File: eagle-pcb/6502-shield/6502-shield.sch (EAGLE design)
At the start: 45 parts, among them SW1 MCSLPT4644B1TR-TACT-SW, SW2 PCM12SMTR-SPDT-RIGHT-ANG, SW3 MCSLPT4644B1TR-TACT-SW, U1 AT28C256TSOP-28, U2 W65C02S, U3 AS6C62256, U4 W65C22, U5 MACHXO-FPGA100TQFP

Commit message: fully routed, getting close
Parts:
- removed D10, D8, D9: ACDC02-41SGWA-DUAL-7SEG, 6502-shield:ACDC02-41SGWA-DUAL-7SEG
- removed R10, R11, R12, R13, R14, R15, R16, R17: 330, rcl:R-US_R0402
- removed U5: MACHXO-FPGA100TQFP, 6502-shield:MACHXO-FPGA100TQFP
- added C1, C2, C5, C6, C7: 0.1uF, rcl:C-USC0402
- added FPGA: MACHXO-FPGA100TQFP, 6502-shield:MACHXO-FPGA100TQFP
- D1, D2, D3, D4, D5, D6, D7: value (none) -> RED
- renumbered SJ1 to J1, SW1 to PB_RESET, SW2 to SW_RUNHALT, SW3 to PB_STEP, U$1 to EXT_XO, U1 to EEPROM, U2 to CPU, U3 to RAM, U4 to PIO
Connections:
- removed net DIGIT1_EN: D8.1EN, U5_BANK1_TOP.PT3D
- removed net DIGIT2_EN: D8.2EN, U5_BANK1_TOP.PT3C
- removed net DIGIT3_EN: D9.1EN, U5_BANK1_TOP.PT3B
- removed net DIGIT4_EN: D9.2EN, U5_BANK1_TOP.PT3A
- removed net DIGIT5_EN: D10.1EN, U5_BANK1_TOP.PT2F
- removed net DIGIT6_EN: D10.2EN, U5_BANK1_TOP.PT2E
- removed net DIGIT_A: R10.2, U5_BANK1_TOP.PT5B
- removed net DIGIT_B: R11.2, U5_BANK1_TOP.PT5A
- removed net DIGIT_C: R12.2, U5_BANK1_TOP.PT4F
- removed net DIGIT_D: R13.2, U5_BANK1_TOP.PT4E
- removed net DIGIT_DP: R17.2, U5_BANK1_TOP.PT4A
- removed net DIGIT_E: R14.2, U5_BANK1_TOP.PT4D
- removed net DIGIT_F: R15.2, U5_BANK1_TOP.PT4C
- removed net DIGIT_G: R16.2, U5_BANK1_TOP.PT4B
- removed net N$23: D10.1A, D10.2A, D8.1A, D8.2A, D9.1A, D9.2A, R10.1
- removed net N$24: D10.1B, D10.2B, D8.1B, D8.2B, D9.1B, D9.2B, R11.1
- removed net N$25: D10.1C, D10.2C, D8.1C, D8.2C, D9.1C, D9.2C, R12.1
- removed net N$26: D10.1D, D10.2D, D8.1D, D8.2D, D9.1D, D9.2D, R13.1
- removed net N$27: D10.1E, D10.2E, D8.1E, D8.2E, D9.1E, D9.2E, R14.1
- removed net N$28: D10.1F, D10.2F, D8.1F, D8.2F, D9.1F, D9.2F, R15.1
- removed net N$29: D10.1G, D10.2G, D8.1G, D8.2G, D9.1G, D9.2G, R16.1
- removed net N$30: D10.1DP, D10.2DP, D8.1DP, D8.2DP, D9.1DP, D9.2DP, R17.1
- removed net ROM_PGM: PCB1.45, U5_BANK0_BOTTOM.PB2D
- new net EEPROM_PGM: FPGA_BANK0_BOTTOM.PB2D, PCB1.23
- net A0: now also FPGA_BANK1_RIGHT.PR8A, PCB1.44; no longer PCB1.22, U5_BANK1_RIGHT.PR8A
- net A1: now also FPGA_BANK1_RIGHT.PR7D, PCB1.45; no longer PCB1.24, U5_BANK1_RIGHT.PR7D
- net A10: now also FPGA_BANK1_RIGHT.PR5A, PCB1.34; no longer PCB1.42, U5_BANK1_RIGHT.PR5A
- net A11: now also FPGA_BANK1_RIGHT.PR4B, PCB1.35; no longer PCB1.44, U5_BANK1_RIGHT.PR4B
- net A12: now also FPGA_BANK1_RIGHT.PR4A, PCB1.32; no longer PCB1.46, U5_BANK1_RIGHT.PR4A
- net A13: now also FPGA_BANK1_RIGHT.PR3D, PCB1.33; no longer PCB1.48, U5_BANK1_RIGHT.PR3D
- net A14: now also FPGA_BANK1_RIGHT.PR3C, PCB1.30; no longer PCB1.50, U5_BANK1_RIGHT.PR3C
- net A15: now also FPGA_BANK1_RIGHT.PR3B, PCB1.31; no longer PCB1.52, U5_BANK1_RIGHT.PR3B
- net A2: now also FPGA_BANK1_RIGHT.PR7C, PCB1.42; no longer PCB1.26, U5_BANK1_RIGHT.PR7C
- net A3: now also FPGA_BANK1_RIGHT.PR7B, PCB1.43; no longer PCB1.28, U5_BANK1_RIGHT.PR7B
- net A4: now also FPGA_BANK1_RIGHT.PR7A, PCB1.40; no longer PCB1.30, U5_BANK1_RIGHT.PR7A
- net A5: now also FPGA_BANK1_RIGHT.PR6B, PCB1.41; no longer PCB1.32, U5_BANK1_RIGHT.PR6B
- net A6: now also FPGA_BANK1_RIGHT.PR6A, PCB1.38; no longer PCB1.34, U5_BANK1_RIGHT.PR6A
- net A7: now also FPGA_BANK1_RIGHT.PR5D, PCB1.39; no longer PCB1.36, U5_BANK1_RIGHT.PR5D
- net A8: now also FPGA_BANK1_RIGHT.PR5C, PCB1.36; no longer PCB1.38, U5_BANK1_RIGHT.PR5C
- net A9: now also FPGA_BANK1_RIGHT.PR5B, PCB1.37; no longer PCB1.40, U5_BANK1_RIGHT.PR5B
- net BE: now also FPGA_BANK0_BOTTOM.PB3C; no longer U5_BANK0_BOTTOM.PB3C
- net CLK: now also FPGA_BANK0_BOTTOM.PB3B, PCB1.27; no longer PCB1.43, U5_BANK0_BOTTOM.PB3B
- net CLK_SEL: now also FPGA_BANK0_LEFT.PL7B; no longer U5_BANK0_LEFT.PL7B
- net D0: now also FPGA_BANK0_BOTTOM.PB4C, PCB1.52; no longer PCB1.23, U5_BANK0_BOTTOM.PB4C
- net D1: now also FPGA_BANK0_BOTTOM.PB4D, PCB1.53; no longer PCB1.25, U5_BANK0_BOTTOM.PB4D
- net D2: now also FPGA_BANK0_BOTTOM.PB5A, PCB1.50; no longer PCB1.27, U5_BANK0_BOTTOM.PB5A
- net D3: now also FPGA_BANK0_BOTTOM.PB5C, PCB1.51; no longer PCB1.29, U5_BANK0_BOTTOM.PB5C
- net D4: now also FPGA_BANK0_BOTTOM.PB5D, PCB1.48; no longer PCB1.31, U5_BANK0_BOTTOM.PB5D
- net D5: now also FPGA_BANK1_RIGHT.PR9B, PCB1.49; no longer PCB1.33, U5_BANK1_RIGHT.PR9B
- net D6: now also FPGA_BANK1_RIGHT.PR9A, PCB1.46; no longer PCB1.35, U5_BANK1_RIGHT.PR9A
- net D7: now also FPGA_BANK1_RIGHT.PR8B, PCB1.47; no longer PCB1.37, U5_BANK1_RIGHT.PR8B
- net DMA: now also FPGA_BANK0_BOTTOM.PB2C, PCB1.22; no longer PCB1.47, U5_BANK0_BOTTOM.PB2C
- net GND: now also C1.2, C2.2, C5.2, C6.2, C7.2, FPGA_CORE.GND; no longer U5_CORE.GND
- net IO_EN: now also FPGA_BANK0_BOTTOM.PB3A; no longer U5_BANK0_BOTTOM.PB3A
- net IRQN: now also FPGA_BANK0_BOTTOM.PB4B; no longer U5_BANK0_BOTTOM.PB4B
- net N$1: now also FPGA_CORE.SLEEPN; no longer U5_CORE.SLEEPN
- net N$10: now also FPGA_BANK0_LEFT.PL2B; no longer U5_BANK0_LEFT.PL2B
- net N$11: now also FPGA_BANK0_LEFT.PL3A; no longer U5_BANK0_LEFT.PL3A
- net N$16: now also FPGA_BANK1_TOP.PT2A; no longer U5_BANK1_TOP.PT2A
- net N$17: now also FPGA_BANK1_TOP.PT2B; no longer U5_BANK1_TOP.PT2B
- net N$18: now also FPGA_BANK1_TOP.PT2C; no longer U5_BANK1_TOP.PT2C
- net N$19: now also FPGA_BANK1_TOP.PT2D; no longer U5_BANK1_TOP.PT2D
- net N$2: now also FPGA_BANK0_LEFT.PL3C; no longer U5_BANK0_LEFT.PL3C
- net N$3: now also FPGA_CORE.GSRN_PL5D; no longer U5_CORE.GSRN_PL5D
- net N$34: now also FPGA_BANK0_LEFT.PL7A; no longer U5_BANK0_LEFT.PL7A
- net N$4: now also FPGA_JTAG.TDO; no longer U5_JTAG.TDO
- net N$5: now also FPGA_JTAG.TMS; no longer U5_JTAG.TMS
- net N$6: now also FPGA_JTAG.TDI; no longer U5_JTAG.TDI
- net N$7: now also FPGA_JTAG.TCK; no longer U5_JTAG.TCK
- net N$8: now also FPGA_BANK0_LEFT.PL3B; no longer U5_BANK0_LEFT.PL3B
- net N$9: now also FPGA_BANK0_LEFT.PL2A; no longer U5_BANK0_LEFT.PL2A
- net OE: now also FPGA_BANK1_RIGHT.PR2B, PCB1.25; no longer PCB1.39, U5_BANK1_RIGHT.PR2B
- net RAM_EN: now also FPGA_BANK1_RIGHT.PR2A; no longer U5_BANK1_RIGHT.PR2A
- net RESETN: now also FPGA_BANK0_BOTTOM.PB3D; no longer U5_BANK0_BOTTOM.PB3D
- net ROM_EN: now also FPGA_BANK1_TOP.PT5C; no longer U5_BANK1_TOP.PT5C
- net RW: now also FPGA_BANK0_BOTTOM.PB4A; no longer U5_BANK0_BOTTOM.PB4A
- net VCC: now also C1.1, C2.1, C5.1, C6.1, C7.1, FPGA_CORE.VCC, FPGA_CORE.VCC_AUX, FPGA_CORE.VCC_IO_0, FPGA_CORE.VCC_IO_1; no longer U5_CORE.VCC, U5_CORE.VCC_AUX, U5_CORE.VCC_IO_0, U5_CORE.VCC_IO_1
- net WE: now also FPGA_BANK1_RIGHT.PR3A, PCB1.29; no longer PCB1.41, U5_BANK1_RIGHT.PR3A
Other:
- moved on the sheet: C3, C4, D3, D4, D6, D7, JP1, R6, R7, R8, R9

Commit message: This should be ready to send out.
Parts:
- EEPROM: value AT28C256TSOP-28 -> AT28BV256TSOP-28; device 6502-shield:AT28C256TSOP-28 -> 6502-shield:AT28BV256TSOP-28
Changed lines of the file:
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@@
 </classes>
 <parts>
-<part name="PCB1" library="E14_Arduino_revC" library_urn="urn:adsk.eagle:library:18477430" deviceset="ARDUINO_MEGA2560" device="" package3d_urn="urn:adsk.eagle:package:18477461/4"/>
+<part name="PCB1" library="E14_Arduino_revC" library_urn="urn:adsk.eagle:library:18477430" deviceset="ARDUINO_MEGA2560" device="" package3d_urn="urn:adsk.eagle:package:18477461/5"/>
 <part name="PB_RESET" library="6502-shield" library_urn="urn:adsk.eagle:library:18477216" deviceset="MCSLPT4644B1TR-TACT-SW" device="" package3d_urn="urn:adsk.eagle:package:18592201/6"/>
 <part name="SW_RUNHALT" library="6502-shield" library_urn="urn:adsk.eagle:library:18477216" deviceset="PCM12SMTR-SPDT-RIGHT-ANG" device="" package3d_urn="urn:adsk.eagle:package:18622137/7"/>
@@
 <part name="P+17" library="supply1" library_urn="urn:adsk.eagle:library:371" deviceset="VCC" device=""/>
 <part name="GND19" library="supply1" library_urn="urn:adsk.eagle:library:371" deviceset="GND" device=""/>
-<part name="EEPROM" library="6502-shield" library_urn="urn:adsk.eagle:library:18477216" deviceset="AT28C256" device="TSOP-28" package3d_urn="urn:adsk.eagle:package:18436546/2"/>
+<part name="EEPROM" library="6502-shield" library_urn="urn:adsk.eagle:library:18477216" deviceset="AT28BV256" device="TSOP-28" package3d_urn="urn:adsk.eagle:package:18436546/2"/>
 <part name="FRAME2" library="frames" library_urn="urn:adsk.eagle:library:229" deviceset="FRAME_A_L" device="" value="6502-shield"/>
 <part name="P+19" library="supply1" library_urn="urn:adsk.eagle:library:371" deviceset="VCC" device=""/>

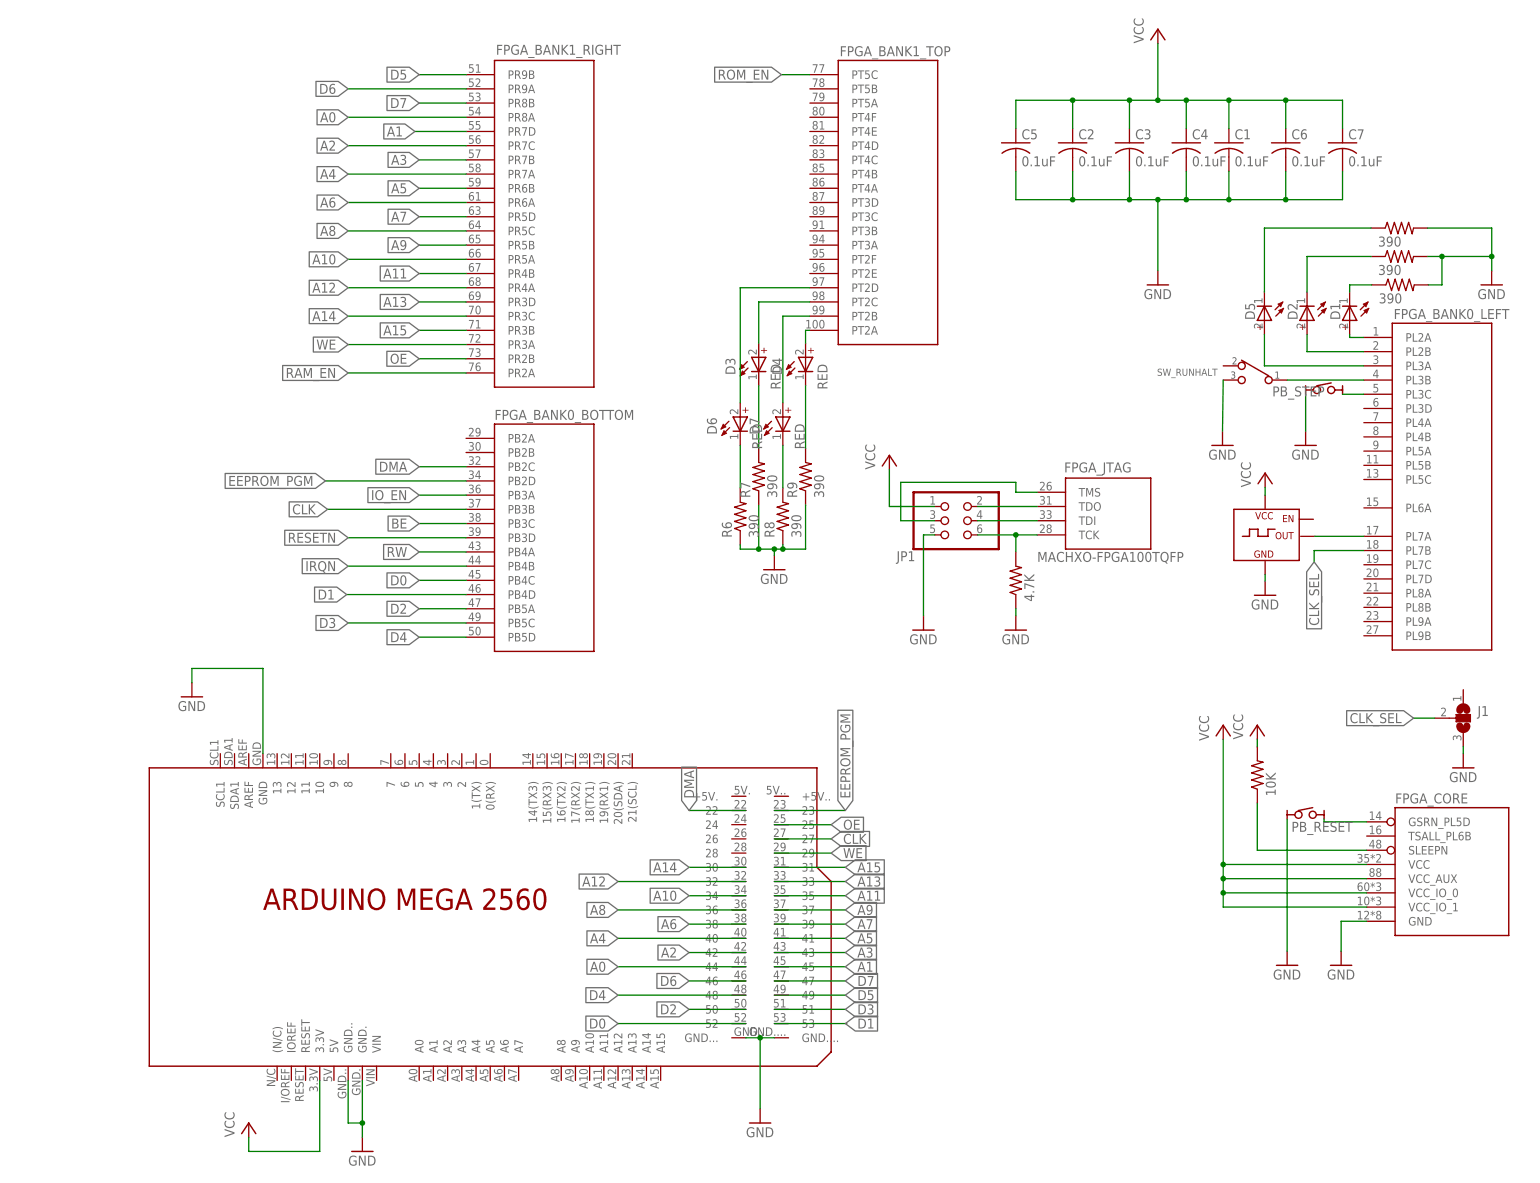
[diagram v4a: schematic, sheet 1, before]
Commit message: Fixed problems with FPGA pinout in component library, updated schematic and cleaned it up a bunch.  Fixed external clock not coming into FPGA on dedicated clock net pin. More schematic work on the list still.
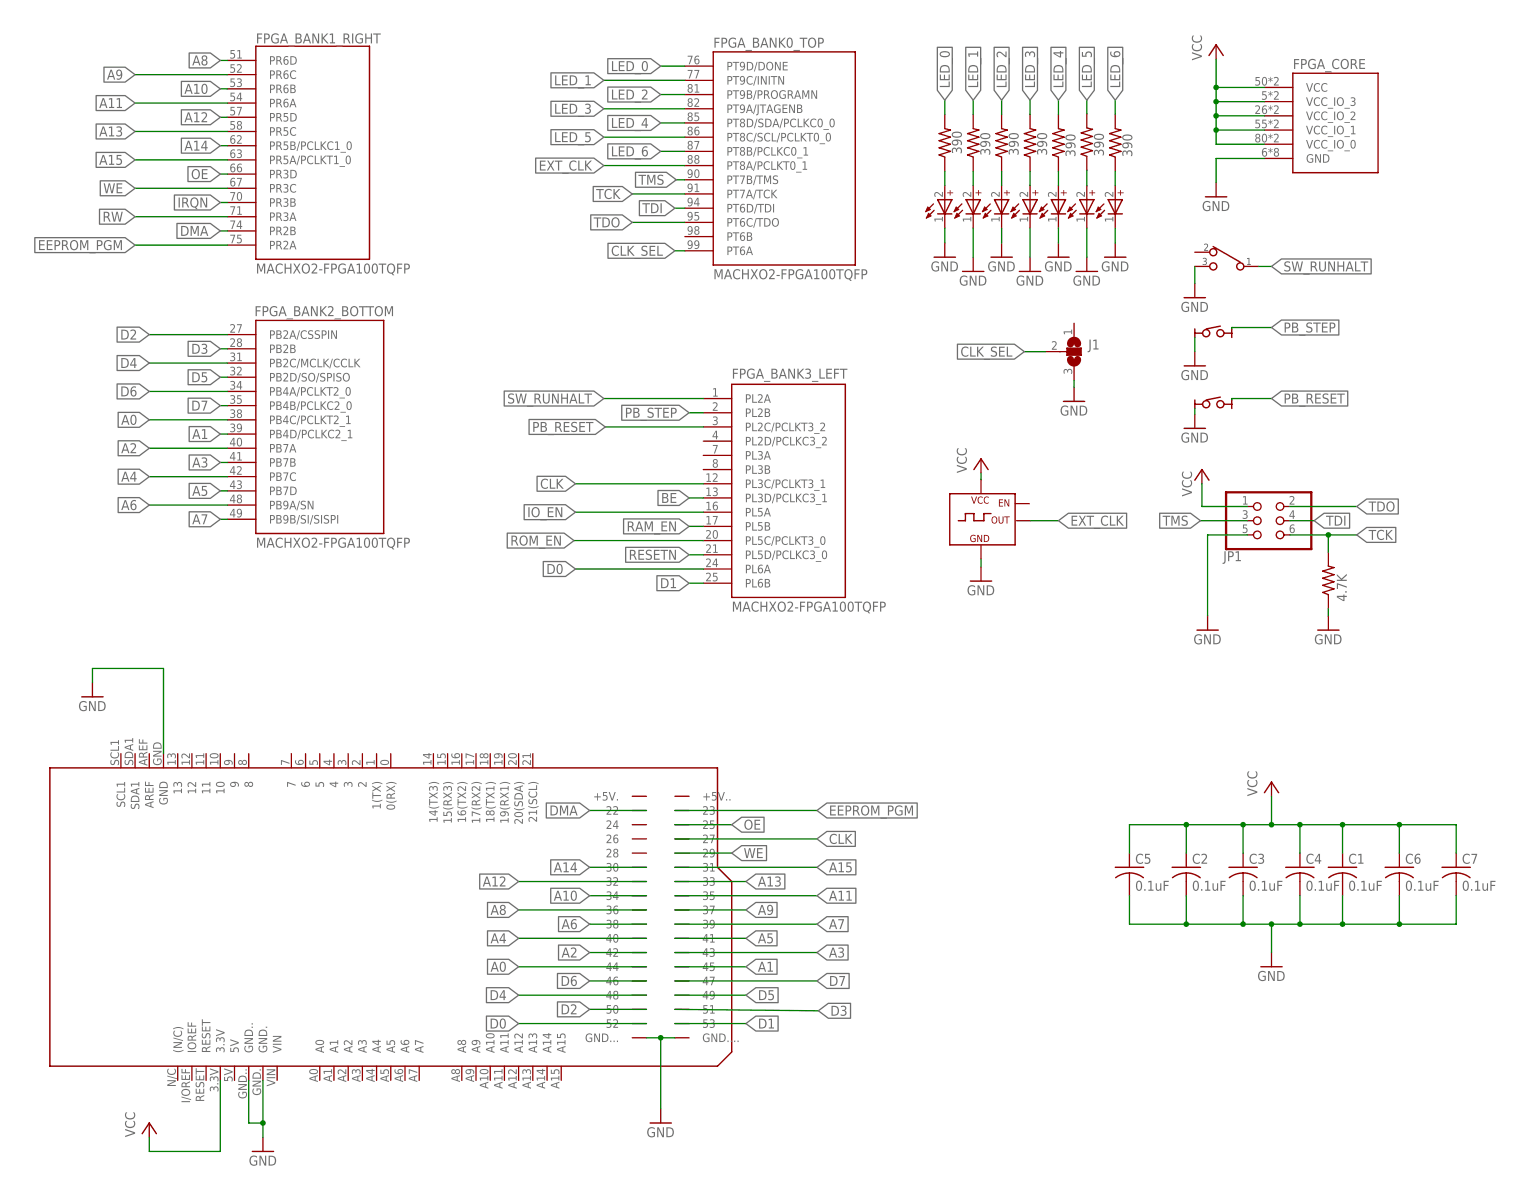
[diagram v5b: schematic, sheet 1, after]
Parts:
- removed R1: 10K, rcl:R-US_R0402
- FPGA: value MACHXO-FPGA100TQFP -> MACHXO2-FPGA100TQFP; device 6502-shield:MACHXO-FPGA100TQFP -> 6502-shield:MACHXO2-FPGA100TQFP
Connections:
- removed net N$1: FPGA_CORE.SLEEPN, R1.1
- removed net N$16: D4.A, FPGA_BANK1_TOP.PT2A
- removed net N$17: D7.A, FPGA_BANK1_TOP.PT2B
- removed net N$18: D3.A, FPGA_BANK1_TOP.PT2C
- removed net N$19: D6.A, FPGA_BANK1_TOP.PT2D
- removed net N$2: FPGA_BANK0_LEFT.PL3C, PB_STEP.T4
- removed net N$20: D1.C, R4.1
- removed net N$21: D2.C, R2.1
- removed net N$22: D5.C, R5.1
- removed net N$3: FPGA_CORE.GSRN_PL5D, PB_RESET.T4
- removed net N$34: EXT_XO.OUT, FPGA_BANK0_LEFT.PL7A
- removed net N$4: FPGA_JTAG.TDO, JP1.2
- removed net N$5: FPGA_JTAG.TMS, JP1.3
- removed net N$6: FPGA_JTAG.TDI, JP1.4
- removed net N$7: FPGA_JTAG.TCK, JP1.6, R3.2
- removed net N$8: FPGA_BANK0_LEFT.PL3B, SW_RUNHALT.1
- new net EXT_CLK: EXT_XO.OUT, FPGA_BANK0_TOP.PT8A/PCLKT0_1
- new net LED_0: FPGA_BANK0_TOP.PT9D/DONE, R5.2
- new net LED_1: FPGA_BANK0_TOP.PT9C/INITN, R6.2
- new net LED_2: FPGA_BANK0_TOP.PT9B/PROGRAMN, R7.2
- new net LED_3: FPGA_BANK0_TOP.PT9A/JTAGENB, R8.2
- new net LED_4: FPGA_BANK0_TOP.PT8D/SDA/PCLKC0_0, R9.2
- new net LED_5: FPGA_BANK0_TOP.PT8C/SCL/PCLKT0_0, R4.2
- new net LED_6: FPGA_BANK0_TOP.PT8B/PCLKC0_1, R2.2
- new net PB_RESET: FPGA_BANK3_LEFT.PL2C/PCLKT3_2, PB_RESET.T3
- new net PB_STEP: FPGA_BANK3_LEFT.PL2B, PB_STEP.T3
- new net SW_RUNHALT: FPGA_BANK3_LEFT.PL2A, SW_RUNHALT.1
- new net TCK: FPGA_BANK0_TOP.PT7A/TCK, JP1.6, R3.2
- new net TDI: FPGA_BANK0_TOP.PT6D/TDI, JP1.4
- new net TDO: FPGA_BANK0_TOP.PT6C/TDO, JP1.2
- new net TMS: FPGA_BANK0_TOP.PT7B/TMS, JP1.3
- net A0: now also FPGA_BANK2_BOTTOM.PB4C/PCLKT2_1; no longer FPGA_BANK1_RIGHT.PR8A
- net A1: now also FPGA_BANK2_BOTTOM.PB4D/PCLKC2_1; no longer FPGA_BANK1_RIGHT.PR7D
- net A10: now also FPGA_BANK1_RIGHT.PR6B; no longer FPGA_BANK1_RIGHT.PR5A
- net A11: now also FPGA_BANK1_RIGHT.PR6A; no longer FPGA_BANK1_RIGHT.PR4B
- net A12: now also FPGA_BANK1_RIGHT.PR5D; no longer FPGA_BANK1_RIGHT.PR4A
- net A13: now also FPGA_BANK1_RIGHT.PR5C; no longer FPGA_BANK1_RIGHT.PR3D
- net A14: now also FPGA_BANK1_RIGHT.PR5B/PCLKC1_0; no longer FPGA_BANK1_RIGHT.PR3C
- net A15: now also FPGA_BANK1_RIGHT.PR5A/PCLKT1_0; no longer FPGA_BANK1_RIGHT.PR3B
- net A2: now also FPGA_BANK2_BOTTOM.PB7A; no longer FPGA_BANK1_RIGHT.PR7C
- net A3: now also FPGA_BANK2_BOTTOM.PB7B; no longer FPGA_BANK1_RIGHT.PR7B
- net A4: now also FPGA_BANK2_BOTTOM.PB7C; no longer FPGA_BANK1_RIGHT.PR7A
- net A5: now also FPGA_BANK2_BOTTOM.PB7D; no longer FPGA_BANK1_RIGHT.PR6B
- net A6: now also FPGA_BANK2_BOTTOM.PB9A/SN; no longer FPGA_BANK1_RIGHT.PR6A
- net A7: now also FPGA_BANK2_BOTTOM.PB9B/SI/SISPI; no longer FPGA_BANK1_RIGHT.PR5D
- net A8: now also FPGA_BANK1_RIGHT.PR6D; no longer FPGA_BANK1_RIGHT.PR5C
- net A9: now also FPGA_BANK1_RIGHT.PR6C; no longer FPGA_BANK1_RIGHT.PR5B
- net BE: now also FPGA_BANK3_LEFT.PL3D/PCLKC3_1; no longer FPGA_BANK0_BOTTOM.PB3C
- net CLK: now also FPGA_BANK3_LEFT.PL3C/PCLKT3_1; no longer FPGA_BANK0_BOTTOM.PB3B
- net CLK_SEL: now also FPGA_BANK0_TOP.PT6A; no longer FPGA_BANK0_LEFT.PL7B
- net D0: now also FPGA_BANK3_LEFT.PL6A; no longer FPGA_BANK0_BOTTOM.PB4C
- net D1: now also FPGA_BANK3_LEFT.PL6B; no longer FPGA_BANK0_BOTTOM.PB4D
- net D2: now also FPGA_BANK2_BOTTOM.PB2A/CSSPIN; no longer FPGA_BANK0_BOTTOM.PB5A
- net D3: now also FPGA_BANK2_BOTTOM.PB2B; no longer FPGA_BANK0_BOTTOM.PB5C
- net D4: now also FPGA_BANK2_BOTTOM.PB2C/MCLK/CCLK; no longer FPGA_BANK0_BOTTOM.PB5D
- net D5: now also FPGA_BANK2_BOTTOM.PB2D/SO/SPISO; no longer FPGA_BANK1_RIGHT.PR9B
- net D6: now also FPGA_BANK2_BOTTOM.PB4A/PCLKT2_0; no longer FPGA_BANK1_RIGHT.PR9A
- net D7: now also FPGA_BANK2_BOTTOM.PB4B/PCLKC2_0; no longer FPGA_BANK1_RIGHT.PR8B
- net DMA: now also FPGA_BANK1_RIGHT.PR2B; no longer FPGA_BANK0_BOTTOM.PB2C
- net EEPROM_PGM: now also FPGA_BANK1_RIGHT.PR2A; no longer FPGA_BANK0_BOTTOM.PB2D
- net GND: now also D1.C, D2.C, D3.C, D4.C, D5.C, D6.C, D7.C; no longer R2.2, R4.2, R5.2, R6.1, R7.1, R8.1, R9.1
- net IO_EN: now also FPGA_BANK3_LEFT.PL5A; no longer FPGA_BANK0_BOTTOM.PB3A
- net IRQN: now also FPGA_BANK1_RIGHT.PR3B; no longer FPGA_BANK0_BOTTOM.PB4B
- net N$10: now also R6.1; no longer FPGA_BANK0_LEFT.PL2B
- net N$11: now also R7.1; no longer FPGA_BANK0_LEFT.PL3A
- net N$12: now also D4.A, R8.1; no longer D6.C, R6.2
- net N$13: now also D3.A, R9.1; no longer D3.C, R7.2
- net N$14: now also D6.A, R4.1; no longer D7.C, R8.2
- net N$15: now also D7.A, R2.1; no longer D4.C, R9.2
- net N$9: now also R5.1; no longer FPGA_BANK0_LEFT.PL2A
- net OE: now also FPGA_BANK1_RIGHT.PR3D; no longer FPGA_BANK1_RIGHT.PR2B
- net RAM_EN: now also FPGA_BANK3_LEFT.PL5B; no longer FPGA_BANK1_RIGHT.PR2A
- net RESETN: now also FPGA_BANK3_LEFT.PL5D/PCLKC3_0; no longer FPGA_BANK0_BOTTOM.PB3D
- net ROM_EN: now also FPGA_BANK3_LEFT.PL5C/PCLKT3_0; no longer FPGA_BANK1_TOP.PT5C
- net RW: now also FPGA_BANK1_RIGHT.PR3A; no longer FPGA_BANK0_BOTTOM.PB4A
- net VCC: now also FPGA_CORE.VCC_IO_2, FPGA_CORE.VCC_IO_3; no longer FPGA_CORE.VCC_AUX, R1.2
- net WE: now also FPGA_BANK1_RIGHT.PR3C; no longer FPGA_BANK1_RIGHT.PR3A
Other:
- moved on the sheet: C1, C2, C3, C4, C5, C6, C7, J1, JP1
